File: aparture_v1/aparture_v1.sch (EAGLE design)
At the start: 89 parts, among them IC1 LD117AS33TR, IC3 LTC1966CMS8, T1 BT138-V, T2 BT138-V, T3 BT138-V, T4 BT138-V, T5 BT138-V, T6 BT138-V, T7 BT138-V, T8 BT138-V

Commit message: brd and sch made for 80*70mm boards, separated controller and triacs
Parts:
- removed C5: C0.22uF, resistor:C-EUC0805
- removed C6: C33pF, resistor:C-EUC0805
- removed C7: C100uF, resistor:CPOL-EU153CLV-0605
- removed C8, C9: C0.1uF, resistor:C-EUC0805
- removed CUR_SENS_JACK: (no value), SparkFun-Connectors:AUDIO-JACKSMD2
- removed D1: (no value), microbuilder:TVSARRAY_5LANE
- removed IC1: LD117AS33TR, v-reg:LD117AS33TR
- removed IC3: LTC1966CMS8, linear-technology-2:LTC1966CMS8
- removed J1: (no value), SparkFun-Connectors:SIMHOLDERSIM
- removed LED1, LED2, LED3, LED4, LED5, LED6, LED7, LED8: (no value), adafruit:LED3MM
- removed LOAD1, LOAD2, LOAD3, LOAD4, LOAD5, LOAD6, LOAD7, LOAD8: (no value), con-ptr500:AK300/2
- removed R1, R12, R15, R18, R21, R24, R6, R9: R120, resistor:R-EU_M0805
- removed R28: R1K, resistor:R-EU_M0805
- removed R4: R100K, resistor:R-EU_M0805
- removed SIM900TEC: 1296-T60, con-leotronics:1296-T60
- removed U$1: ARDUINO_PRO_MINI, tigorcustom:ARDUINO_PRO_MINI
- removed VOL_REG_SIM900: DCDCMODULE, bontor:DCDCMODULE
- added IN, OUT: (no value), con-ptr500:AK300/10
- added JP3: SMPS_OUT, pinhead:PINHD-1X2
- added OK10, OK9: MOC3021M, optocoupler:MOC3021M
- added T10: BT138-V, triac:BT138-V
- C1, C2: value C10uF -> C0.1uF
- JP2: value SMPS_OUT -> (none); device pinhead:PINHD-1X2 -> pinhead:PINHD-2X5
- R27: value R50 -> R2.4K
- R29: value R2K -> R180
- R30: value R120 -> R2.4K
- R5: value R100K -> R180
- T9: value (none) -> BT138-V; device transistor-neu-to92:MMBT2222ALT1-NPN-SOT23-BEC -> triac:BT138-V
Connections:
- removed net 3V3: C2.1, IC1.OUT, IC3P.VDD, LED1.A, LED2.A, LED3.A, LED4.A, LED5.A, LED6.A, LED7.A, LED8.A, R4.2, U$1.VCC
- removed net CTRL_PWRKEY: R30.1, U$1.A2
- removed net CUR_SENS: CUR_SENS_JACK.RIGHT, IC3G$1.IN1, R27.2
- removed net CUR_SENS_DC: C9.1, IC3G$1.VOUT, U$1.A3
- removed net N$1: LED1.C, R1.1
- removed net N$10: LED2.C, R6.1
- removed net N$11: OK2.A, R6.2
- removed net N$16: LED3.C, R9.1
- removed net N$17: OK3.A, R9.2
- removed net N$2: OK1.A, R1.2
- removed net N$22: LED4.C, R12.1
- removed net N$23: OK4.A, R12.2
- removed net N$28: LED5.C, R15.1
- removed net N$29: OK5.A, R15.2
- removed net N$34: LED6.C, R18.1
- removed net N$35: OK6.A, R18.2
- removed net N$40: LED7.C, R21.1
- removed net N$41: OK7.A, R21.2
- removed net N$46: LED8.C, R24.1
- removed net N$47: OK8.A, R24.2
- removed net N$7: C8.1, IC3G$1.IN2, R27.1, R4.1, R5.2
- removed net N$8: R30.2, T9.B
- removed net PWRKEY: SIM900TEC-17.B, T9.C
- removed net SIM_CLK: D1.C4, J1.CLK, SIM900TEC-31.B
- removed net SIM_DATA: D1.C3, J1.I/O, SIM900TEC-29.B
- removed net SIM_RST: D1.C2, J1.RST, SIM900TEC-27.B
- removed net SIM_RXD: SIM900TEC-41.B, U$1.TXO
- removed net SIM_TXD: R28.2, SIM900TEC-43.B
- removed net SIM_TXD_L: R28.1, R29.2, U$1.RXI
- removed net SIM_VDD: C5.1, C6.1, D1.C1, J1.VCC, SIM900TEC-25.B
- removed net VBAT: C7.+, SIM900TEC-1.B, SIM900TEC-3.B, SIM900TEC-5.B, SIM900TEC-7.B, SIM900TEC-9.B, VOL_REG_SIM900.VOUT
- new net CTRL_SW10: JP2.10, OK10.C
- new net CTRL_SW9: JP2.9, OK9.C
- new net N$52: IN-2.KL, R8.2, T2.A2
- new net N$53: IN-3.KL, R11.2, T3.A2
- new net N$54: IN-4.KL, R14.2, T4.A2
- new net N$55: IN-8.KL, R26.2, T8.A2
- new net N$56: IN-7.KL, R23.2, T7.A2
- new net N$57: IN-6.KL, R20.2, T6.A2
- new net N$58: IN-5.KL, R17.2, T5.A2
- new net N$59: OK9.A2, R5.1
- new net N$60: C1.1, R27.1, R5.2
- new net N$61: OK9.A1, T9.G
- new net N$62: C1.2, OUT-9.KL, T9.A1
- new net N$65: OK10.A2, R29.1
- new net N$66: C2.1, R29.2, R30.1
- new net N$67: OK10.A1, T10.G
- new net N$68: C2.2, OUT-10.KL, T10.A1
- new net N$69: IN-9.KL, R27.2, T9.A2
- new net N$70: IN-10.KL, R30.2, T10.A2
- new net N$9: IN-1.KL, R3.2, T1.A2
- net AC_IN: no longer R11.2, R14.2, R17.2, R20.2, R23.2, R26.2, R3.2, R8.2, T1.A2, T2.A2, T3.A2, T4.A2, T5.A2, T6.A2, T7.A2, T8.A2
- net CTRL_SW1: now also JP2.1; no longer U$1.2
- net CTRL_SW2: now also JP2.2; no longer U$1.*3
- net CTRL_SW3: now also JP2.3; no longer U$1.4
- net CTRL_SW4: now also JP2.4; no longer U$1.*5
- net CTRL_SW5: now also JP2.5; no longer U$1.*6
- net CTRL_SW6: now also JP2.6; no longer U$1.7
- net CTRL_SW7: now also JP2.7; no longer U$1.8
- net CTRL_SW8: now also JP2.8; no longer U$1.*9
- net GND: now also JP3.1; no longer C1.2, C2.2, C5.2, C6.2, C7.-, C8.2, C9.2, CUR_SENS_JACK.SLEEVE, D1.A, IC1.ADJ, IC3G$1./EN, IC3G$1.RTN, IC3P.GND, IC3P.VSS, J1.GND, JP2.1, R29.1, R5.1, SIM900TEC-10.B, SIM900TEC-2.B, SIM900TEC-4.B, SIM900TEC-51.B, SIM900TEC-52.B, SIM900TEC-6.B, SIM900TEC-8.B, T9.E, U$1.GND, U$1.GND@2, VOL_REG_SIM900.GNDI, VOL_REG_SIM900.GNDO
- net N$15: now also OUT-2.KL; no longer LOAD2-1.KL
- net N$21: now also OUT-3.KL; no longer LOAD3-1.KL
- net N$27: now also OUT-4.KL; no longer LOAD4-1.KL
- net N$33: now also OUT-5.KL; no longer LOAD5-1.KL
- net N$39: now also OUT-6.KL; no longer LOAD6-1.KL
- net N$45: now also OUT-7.KL; no longer LOAD7-1.KL
- net N$51: now also OUT-8.KL; no longer LOAD8-1.KL
- net N$6: now also OUT-1.KL; no longer LOAD1-1.KL
- net NEUTRAL: no longer LOAD1-2.KL, LOAD2-2.KL, LOAD3-2.KL, LOAD4-2.KL, LOAD5-2.KL, LOAD6-2.KL, LOAD7-2.KL, LOAD8-2.KL
- net VDC: now also JP3.2, OK1.A, OK10.A, OK2.A, OK3.A, OK4.A, OK5.A, OK6.A, OK7.A, OK8.A, OK9.A; no longer C1.1, IC1.IN, JP2.2, VOL_REG_SIM900.VIN
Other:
- note removed: "Controller"
- note removed: "Current Sensing"
- note removed: "SIM900"
- moved on the sheet: C1, C10, C11, C12, C13, C14, C15, C16, C2, C3, JP1, MAINS-1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

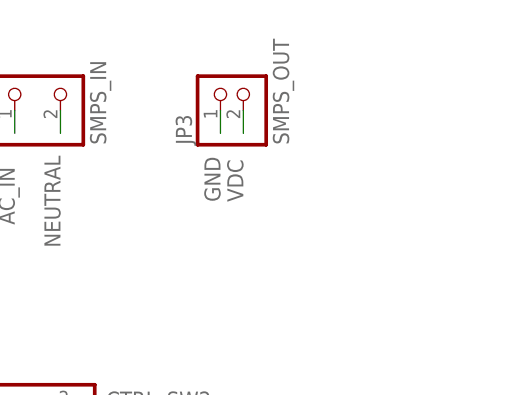
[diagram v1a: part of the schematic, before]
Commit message: resize boards
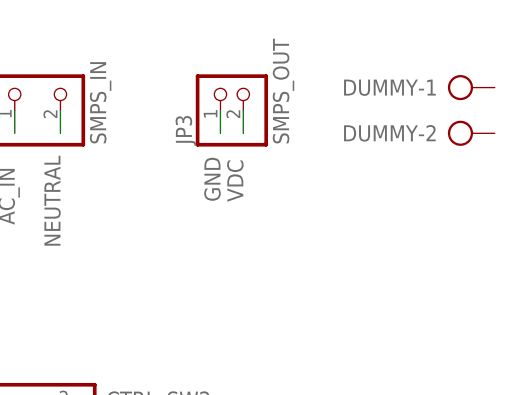
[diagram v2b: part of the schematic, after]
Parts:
- added DUMMY: (no value), con-ptr500:AK300/2
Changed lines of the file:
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@@
 <grid distance="0.1" unitdist="inch" unit="inch" style="lines" multiple="1" display="no" altdistance="0.01" altunitdist="inch" altunit="inch"/>
 <layers>
-<layer number="1" name="Top" color="4" fill="1" visible="yes" active="no"/>
-<layer number="2" name="Route2" color="1" fill="3" visible="yes" active="no"/>
-<layer number="3" name="Route3" color="4" fill="3" visible="yes" active="no"/>
-<layer number="4" name="Route4" color="1" fill="4" visible="yes" active="no"/>
-<layer number="5" name="Route5" color="4" fill="4" visible="yes" active="no"/>
-<layer number="6" name="Route6" color="1" fill="8" visible="yes" active="no"/>
-<layer number="7" name="Route7" color="4" fill="8" visible="yes" active="no"/>
-<layer number="8" name="Route8" color="1" fill="2" visible="yes" active="no"/>
-<layer number="9" name="Route9" color="4" fill="2" visible="yes" active="no"/>
-<layer number="10" name="Route10" color="1" fill="7" visible="yes" active="no"/>
-<layer number="11" name="Route11" color="4" fill="7" visible="yes" active="no"/>
-<layer number="12" name="Route12" color="1" fill="5" visible="yes" active="no"/>
-<layer number="13" name="Route13" color="4" fill="5" visible="yes" active="no"/>
-<layer number="14" name="Route14" color="1" fill="6" visible="yes" active="no"/>
-<layer number="15" name="Route15" color="4" fill="6" visible="yes" active="no"/>
-<layer number="16" name="Bottom" color="1" fill="1" visible="yes" active="no"/>
-<layer number="17" name="Pads" color="2" fill="1" visible="yes" active="no"/>
-<layer number="18" name="Vias" color="2" fill="1" visible="yes" active="no"/>
-<layer number="19" name="Unrouted" color="6" fill="1" visible="yes" active="no"/>
-<layer number="20" name="Dimension" color="15" fill="1" visible="yes" active="no"/>
-<layer number="21" name="tPlace" color="7" fill="1" visible="yes" active="no"/>
-<layer number="22" name="bPlace" color="7" fill="1" visible="yes" active="no"/>
-<layer number="23" name="tOrigins" color="15" fill="1" visible="yes" active="no"/>
-<layer number="24" name="bOrigins" color="15" fill="1" visible="yes" active="no"/>
-<layer number="25" name="tNames" color="7" fill="1" visible="yes" active="no"/>
-<layer number="26" name="bNames" color="7" fill="1" visible="yes" active="no"/>
-<layer number="27" name="tValues" color="7" fill="1" visible="yes" active="no"/>
-<layer number="28" name="bValues" color="7" fill="1" visible="yes" active="no"/>
+<layer number="1" name="Top" color="4" fill="1" visible="no" active="no"/>
+<layer number="2" name="Route2" color="1" fill="3" visible="no" active="no"/>
+<layer number="3" name="Route3" color="4" fill="3" visible="no" active="no"/>
+<layer number="4" name="Route4" color="1" fill="4" visible="no" active="no"/>
+<layer number="5" name="Route5" color="4" fill="4" visible="no" active="no"/>
+<layer number="6" name="Route6" color="1" fill="8" visible="no" active="no"/>
+<layer number="7" name="Route7" color="4" fill="8" visible="no" active="no"/>
+<layer number="8" name="Route8" color="1" fill="2" visible="no" active="no"/>
+<layer number="9" name="Route9" color="4" fill="2" visible="no" active="no"/>
+<layer number="10" name="Route10" color="1" fill="7" visible="no" active="no"/>
+<layer number="11" name="Route11" color="4" fill="7" visible="no" active="no"/>
+<layer number="12" name="Route12" color="1" fill="5" visible="no" active="no"/>
+<layer number="13" name="Route13" color="4" fill="5" visible="no" active="no"/>
+<layer number="14" name="Route14" color="1" fill="6" visible="no" active="no"/>
+<layer number="15" name="Route15" color="4" fill="6" visible="no" active="no"/>
+<layer number="16" name="Bottom" color="1" fill="1" visible="no" active="no"/>
+<layer number="17" name="Pads" color="2" fill="1" visible="no" active="no"/>
+<layer number="18" name="Vias" color="2" fill="1" visible="no" active="no"/>
+<layer number="19" name="Unrouted" color="6" fill="1" visible="no" active="no"/>
+<layer number="20" name="Dimension" color="15" fill="1" visible="no" active="no"/>
+<layer number="21" name="tPlace" color="7" fill="1" visible="no" active="no"/>
+<layer number="22" name="bPlace" color="7" fill="1" visible="no" active="no"/>
+<layer number="23" name="tOrigins" color="15" fill="1" visible="no" active="no"/>
+<layer number="24" name="bOrigins" color="15" fill="1" visible="no" active="no"/>
+<layer number="25" name="tNames" color="7" fill="1" visible="no" active="no"/>
+<layer number="26" name="bNames" color="7" fill="1" visible="no" active="no"/>
+<layer number="27" name="tValues" color="7" fill="1" visible="no" active="no"/>
+<layer number="28" name="bValues" color="7" fill="1" visible="no" active="no"/>
 <layer number="29" name="tStop" color="7" fill="3" visible="no" active="no"/>
 <layer number="30" name="bStop" color="7" fill="6" visible="no" active="no"/>
@@
 <layer number="35" name="tGlue" color="7" fill="4" visible="no" active="no"/>
 <layer number="36" name="bGlue" color="7" fill="5" visible="no" active="no"/>
-<layer number="37" name="tTest" color="7" fill="1" visible="yes" active="no"/>
-<layer number="38" name="bTest" color="7" fill="1" visible="yes" active="no"/>
+<layer number="37" name="tTest" color="7" fill="1" visible="no" active="no"/>
+<layer number="38" name="bTest" color="7" fill="1" visible="no" active="no"/>
 <layer number="39" name="tKeepout" color="4" fill="11" visible="no" active="no"/>
 <layer number="40" name="bKeepout" color="1" fill="11" visible="no" active="no"/>
@@
 <layer number="44" name="Drills" color="7" fill="1" visible="no" active="no"/>
 <layer number="45" name="Holes" color="7" fill="1" visible="no" active="no"/>
-<layer number="46" name="Milling" color="3" fill="1" visible="yes" active="no"/>
-<layer number="47" name="Measures" color="7" fill="1" visible="yes" active="no"/>
-<layer number="48" name="Document" color="7" fill="1" visible="yes" active="no"/>
-<layer number="49" name="Reference" color="7" fill="1" visible="yes" active="no"/>
-<layer number="50" name="dxf" color="7" fill="1" visible="yes" active="no"/>
-<layer number="51" name="tDocu" color="7" fill="1" visible="yes" active="no"/>
-<layer number="52" name="bDocu" color="7" fill="1" visible="yes" active="no"/>
-<layer number="53" name="tGND_GNDA" color="7" fill="9" visible="yes" active="no"/>
-<layer number="54" name="bGND_GNDA" color="1" fill="9" visible="yes" active="no"/>
-<layer number="56" name="wert" color="7" fill="1" visible="yes" active="no"/>
-<layer number="57" name="tCAD" color="7" fill="1" visible="yes" active="no"/>
+<layer number="46" name="Milling" color="3" fill="1" visible="no" active="no"/>
+<layer number="47" name="Measures" color="7" fill="1" visible="no" active="no"/>
+<layer number="48" name="Document" color="7" fill="1" visible="no" active="no"/>
+<layer number="49" name="Reference" color="7" fill="1" visible="no" active="no"/>
+<layer number="50" name="dxf" color="7" fill="1" visible="no" active="no"/>
+<layer number="51" name="tDocu" color="7" fill="1" visible="no" active="no"/>
+<layer number="52" name="bDocu" color="7" fill="1" visible="no" active="no"/>
+<layer number="53" name="tGND_GNDA" color="7" fill="9" visible="no" active="no"/>
+<layer number="54" name="bGND_GNDA" color="1" fill="9" visible="no" active="no"/>
+<layer number="56" name="wert" color="7" fill="1" visible="no" active="no"/>
+<layer number="57" name="tCAD" color="7" fill="1" visible="no" active="no"/>
 <layer number="91" name="Nets" color="2" fill="1" visible="yes" active="yes"/>
 <layer number="92" name="Busses" color="1" fill="1" visible="yes" active="yes"/>
@@
 <part name="JP2" library="pinhead" deviceset="PINHD-2X5" device=""/>
 <part name="JP3" library="pinhead" deviceset="PINHD-1X2" device="" value="SMPS_OUT"/>
+<part name="DUMMY" library="con-ptr500" deviceset="AK300/2" device="">
+<attribute name="MF" value=""/>
+<attribute name="MPN" value=""/>
+<attribute name="OC_FARNELL" value="unknown"/>
+<attribute name="OC_NEWARK" value="unknown"/>
+</part>
 </parts>
 <sheets>
@@
 <instance part="JP2" gate="A" x="241.3" y="172.72"/>
 <instance part="JP3" gate="G$1" x="266.7" y="213.36" rot="R90"/>
+<instance part="DUMMY" gate="-1" x="289.56" y="213.36"/>
+<instance part="DUMMY" gate="-2" x="289.56" y="208.28"/>
 </instances>
 <busses>
